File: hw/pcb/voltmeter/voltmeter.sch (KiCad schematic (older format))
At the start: 32 parts, among them J0 1935161, Q1 2N7002, Q2 2N7002, U1 SN74HC595DR, U2 TL062

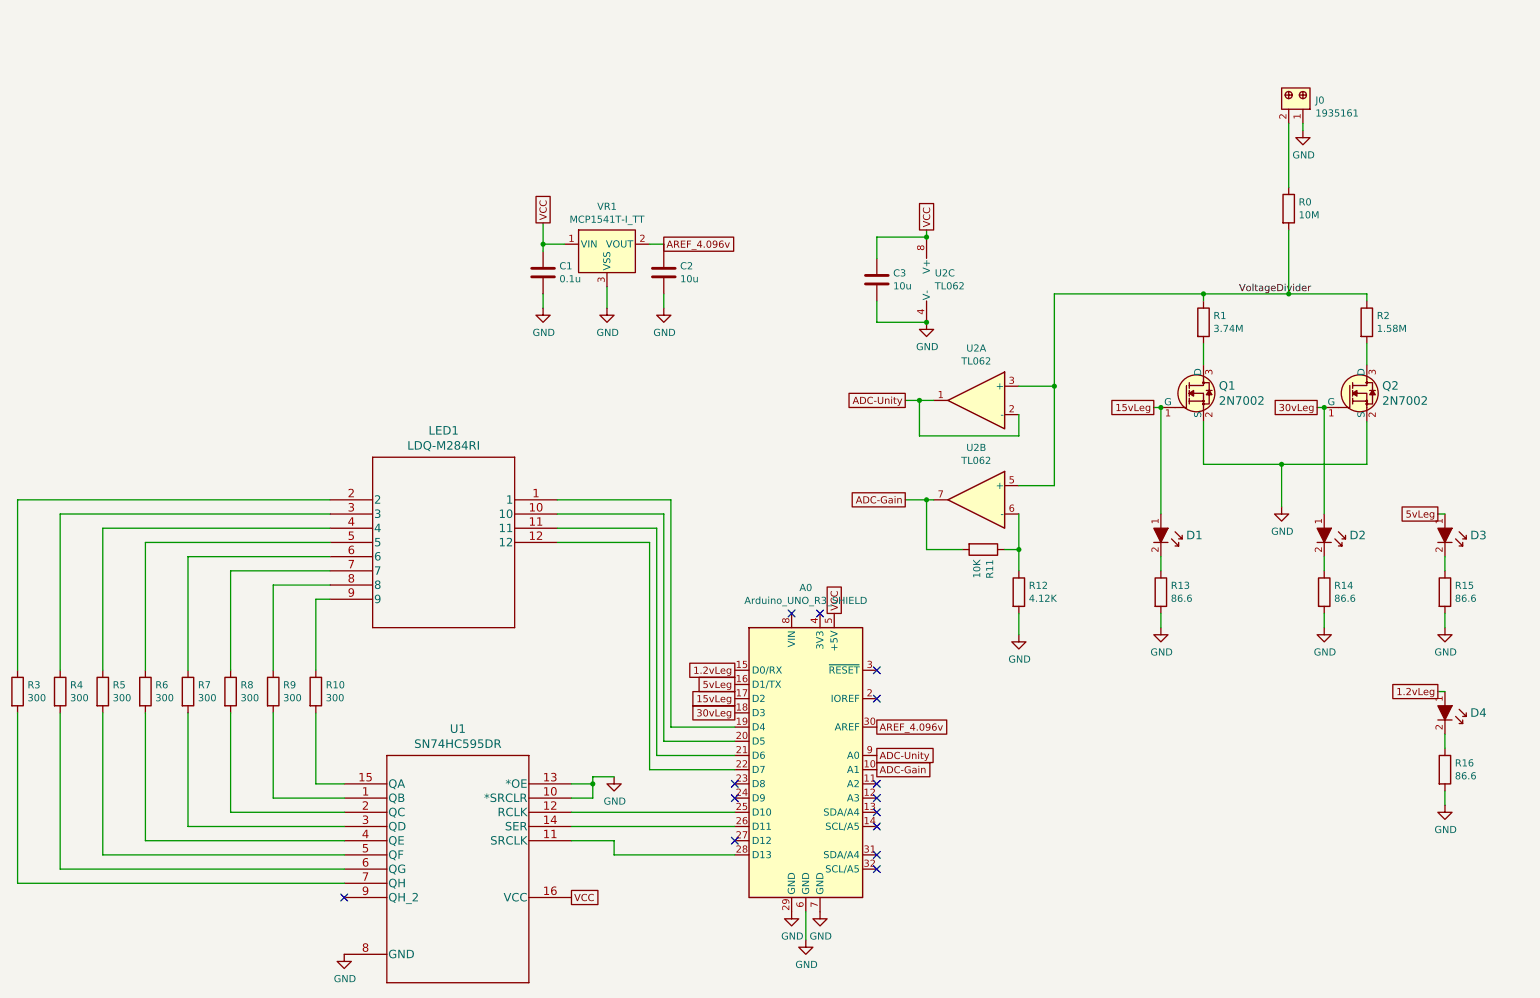
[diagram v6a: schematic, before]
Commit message: Fix incorrect 7-segment pinout.
Fixed bad 7-segment pinout. Fixed layout; regenerated gerbers.
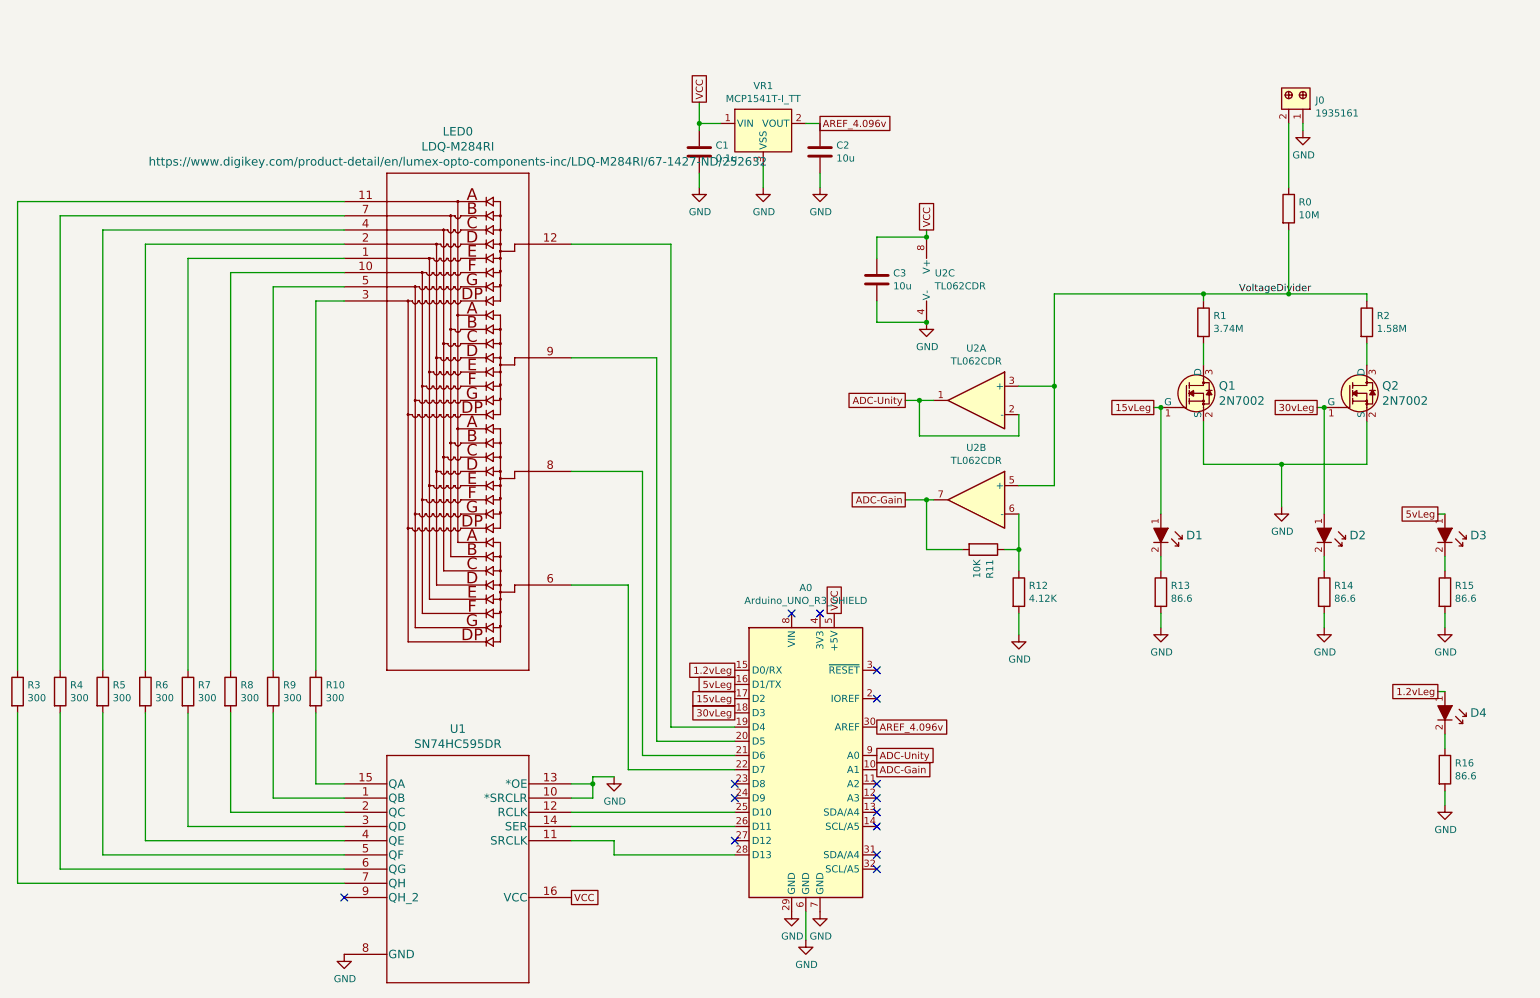
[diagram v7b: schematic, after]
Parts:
- removed LED1: LDQ-M284RI, footprints3:LDQ-M284RI, symbol 2020-08-31_02-39-33:LDQ-M284RI
- added LED0: LDQ-M284RI, footprints4:LDQ-M284RI, symbol 2020-09-17_03-48-59:LDQ-M284RI
- U2: value TL062 -> TL062CDR
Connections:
- net at A0.19 (D4): now also LED0.12
- net at A0.20 (D5): now also LED0.9
- net at A0.21 (D6): now also LED0.8
- net at A0.22 (D7): now also LED0.6
- net at R3.1: now also LED0.11
- net at R4.1: now also LED0.7
- net at R5.1: now also LED0.4
- net at R6.1: now also LED0.2
- net at R7.1: now also LED0.1
- net at R8.1: now also LED0.10
- net at R9.1: now also LED0.5
- net at R10.1: now also LED0.3
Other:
- moved on the sheet: C1, C2, VR1
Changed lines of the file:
@@
 L dk_PMIC-Voltage-Reference:MCP1541T-I_TT VR1
 U 1 1 5F4868C2
-P 4750 1700
-F 0 "VR1" H 4750 1965 50  0000 C CNN
-F 1 "MCP1541T-I_TT" H 4750 1874 50  0000 C CNN
-F 2 "digikey-footprints:SOT-23-3" H 4950 1900 60  0001 L CNN
-F 3 "http://www.microchip.com/mymicrochip/filehandler.aspx?ddocname=en011331" H 4950 2000 60  0001 L CNN
-F 4 "MCP1541T-I/TTCT-ND" H 4950 2100 60  0001 L CNN "Digi-Key_PN"
-F 5 "MCP1541T-I/TT" H 4950 2200 60  0001 L CNN "MPN"
-F 6 "Integrated Circuits (ICs)" H 4950 2300 60  0001 L CNN "Category"
-F 7 "PMIC - Voltage Reference" H 4950 2400 60  0001 L CNN "Family"
-F 8 "http://www.microchip.com/mymicrochip/filehandler.aspx?ddocname=en011331" H 4950 2500 60  0001 L CNN "DK_Datasheet_Link"
-F 9 "/product-detail/en/microchip-technology/MCP1541T-I-TT/MCP1541T-I-TTCT-ND/1979818" H 4950 2600 60  0001 L CNN "DK_Detail_Page"
-F 10 "IC VREF SERIES 4.096V SOT23-3" H 4950 2700 60  0001 L CNN "Description"
-F 11 "Microchip Technology" H 4950 2800 60  0001 L CNN "Manufacturer"
-F 12 "Active" H 4950 2900 60  0001 L CNN "Status"
-	1    4750 1700
+P 5850 850
+F 0 "VR1" H 5850 1115 50  0000 C CNN
+F 1 "MCP1541T-I_TT" H 5850 1024 50  0000 C CNN
+F 2 "digikey-footprints:SOT-23-3" H 6050 1050 60  0001 L CNN
+F 3 "http://www.microchip.com/mymicrochip/filehandler.aspx?ddocname=en011331" H 6050 1150 60  0001 L CNN
+F 4 "MCP1541T-I/TTCT-ND" H 6050 1250 60  0001 L CNN "Digi-Key_PN"
+F 5 "MCP1541T-I/TT" H 6050 1350 60  0001 L CNN "MPN"
+F 6 "Integrated Circuits (ICs)" H 6050 1450 60  0001 L CNN "Category"
+F 7 "PMIC - Voltage Reference" H 6050 1550 60  0001 L CNN "Family"
+F 8 "http://www.microchip.com/mymicrochip/filehandler.aspx?ddocname=en011331" H 6050 1650 60  0001 L CNN "DK_Datasheet_Link"
+F 9 "/product-detail/en/microchip-technology/MCP1541T-I-TT/MCP1541T-I-TTCT-ND/1979818" H 6050 1750 60  0001 L CNN "DK_Detail_Page"
+F 10 "IC VREF SERIES 4.096V SOT23-3" H 6050 1850 60  0001 L CNN "Description"
+F 11 "Microchip Technology" H 6050 1950 60  0001 L CNN "Manufacturer"
+F 12 "Active" H 6050 2050 60  0001 L CNN "Status"
+	1    5850 850
 	1    0    0    -1
 $EndComp
@@
 P 7350 2800
 F 0 "U2" H 7350 3167 50  0000 C CNN
-F 1 "TL062" H 7350 3076 50  0000 C CNN
+F 1 "TL062CDR" H 7350 3076 50  0000 C CNN
 F 2 "footprints:TL062CDR" H 7350 2800 50  0001 C CNN
-F 3 "http://www.ti.com/lit/ds/symlink/tl061.pdf" H 7350 2800 50  0001 C CNN
+F 3 "https://www.digikey.com/product-detail/en/texas-instruments/TL062CDR/296-1281-1-ND/276549" H 7350 2800 50  0001 C CNN
 	1    7350 2800
 	-1   0    0    -1
@@
 P 7350 3500
 F 0 "U2" H 7350 3867 50  0000 C CNN
-F 1 "TL062" H 7350 3776 50  0000 C CNN
+F 1 "TL062CDR" H 7350 3776 50  0000 C CNN
 F 2 "footprints:TL062CDR" H 7350 3500 50  0001 C CNN
-F 3 "http://www.ti.com/lit/ds/symlink/tl061.pdf" H 7350 3500 50  0001 C CNN
+F 3 "https://www.digikey.com/product-detail/en/texas-instruments/TL062CDR/296-1281-1-ND/276549" H 7350 3500 50  0001 C CNN
 	2    7350 3500
 	-1   0    0    -1
@@
 P 7100 1950
 F 0 "U2" H 7058 1996 50  0000 L CNN
-F 1 "TL062" H 7058 1905 50  0000 L CNN
+F 1 "TL062CDR" H 7058 1905 50  0000 L CNN
 F 2 "footprints:TL062CDR" H 7100 1950 50  0001 C CNN
-F 3 "http://www.ti.com/lit/ds/symlink/tl061.pdf" H 7100 1950 50  0001 C CNN
+F 3 "https://www.digikey.com/product-detail/en/texas-instruments/TL062CDR/296-1281-1-ND/276549" H 7100 1950 50  0001 C CNN
 	3    7100 1950
 	1    0    0    -1
@@
 L Device:C C1
 U 1 1 5F4C5E92
-P 4300 1900
-F 0 "C1" H 4415 1946 50  0000 L CNN
-F 1 "0.1u" H 4415 1855 50  0000 L CNN
-F 2 "Capacitor_SMD:C_0805_2012Metric_Pad1.15x1.40mm_HandSolder" H 4338 1750 50  0001 C CNN
-F 3 "~" H 4300 1900 50  0001 C CNN
-	1    4300 1900
+P 5400 1050
+F 0 "C1" H 5515 1096 50  0000 L CNN
+F 1 "0.1u" H 5515 1005 50  0000 L CNN
+F 2 "Capacitor_SMD:C_0805_2012Metric_Pad1.15x1.40mm_HandSolder" H 5438 900 50  0001 C CNN
+F 3 "~" H 5400 1050 50  0001 C CNN
+	1    5400 1050
 	1    0    0    -1
 $EndComp
@@
 L Device:C C2
 U 1 1 5F4C90BC
-P 5150 1900
-F 0 "C2" H 5265 1946 50  0000 L CNN
-F 1 "10u" H 5265 1855 50  0000 L CNN
-F 2 "Capacitor_SMD:C_0805_2012Metric_Pad1.15x1.40mm_HandSolder" H 5188 1750 50  0001 C CNN
-F 3 "~" H 5150 1900 50  0001 C CNN
-	1    5150 1900
+P 6250 1050
+F 0 "C2" H 6365 1096 50  0000 L CNN
+F 1 "10u" H 6365 1005 50  0000 L CNN
+F 2 "Capacitor_SMD:C_0805_2012Metric_Pad1.15x1.40mm_HandSolder" H 6288 900 50  0001 C CNN
+F 3 "~" H 6250 1050 50  0001 C CNN
+	1    6250 1050
 	1    0    0    -1
 $EndComp
@@
 L power:GND #PWR0109
 U 1 1 5F4CBE9E
-P 4750 2150
-F 0 "#PWR0109" H 4750 1900 50  0001 C CNN
-F 1 "GND" H 4755 1977 50  0000 C CNN
-F 2 "" H 4750 2150 50  0001 C CNN
-F 3 "" H 4750 2150 50  0001 C CNN
-	1    4750 2150
+P 5850 1300
+F 0 "#PWR0109" H 5850 1050 50  0001 C CNN
+F 1 "GND" H 5855 1127 50  0000 C CNN
+F 2 "" H 5850 1300 50  0001 C CNN
+F 3 "" H 5850 1300 50  0001 C CNN
+	1    5850 1300
 	1    0    0    -1
 $EndComp
@@
 	1    0    0    -1
 $EndComp
-Text GLabel 4300 1550 1    50   UnSpc ~ 0
+Text GLabel 5400 700  1    50   UnSpc ~ 0
 VCC
 Wire Wire Line
-	4300 1550 4300 1700
-Wire Wire Line
-	4450 1700 4300 1700
-Connection ~ 4300 1700
-Wire Wire Line
-	4300 1700 4300 1750
-Wire Wire Line
-	4300 2050 4300 2150
-Wire Wire Line
-	4750 2000 4750 2150
+	5400 700  5400 850
+Wire Wire Line
+	5550 850  5400 850
+Connection ~ 5400 850
+Wire Wire Line
+	5400 850  5400 900
+Wire Wire Line
+	5400 1200 5400 1300
+Wire Wire Line
+	5850 1150 5850 1300
 $Comp
 L power:GND #PWR0111
 U 1 1 5F4D0D65
-P 5150 2150
-F 0 "#PWR0111" H 5150 1900 50  0001 C CNN
-F 1 "GND" H 5155 1977 50  0000 C CNN
-F 2 "" H 5150 2150 50  0001 C CNN
-F 3 "" H 5150 2150 50  0001 C CNN
-	1    5150 2150
-	1    0    0    -1
-$EndComp
-Wire Wire Line
-	5050 1700 5150 1700
-Wire Wire Line
-	5150 1700 5150 1750
-Wire Wire Line
-	5150 2050 5150 2150
-Text GLabel 5150 1700 2    50   UnSpc ~ 0
+P 6250 1300
+F 0 "#PWR0111" H 6250 1050 50  0001 C CNN
+F 1 "GND" H 6255 1127 50  0000 C CNN
+F 2 "" H 6250 1300 50  0001 C CNN
+F 3 "" H 6250 1300 50  0001 C CNN
+	1    6250 1300
+	1    0    0    -1
+$EndComp
+Wire Wire Line
+	6150 850  6250 850
+Wire Wire Line
+	6250 850  6250 900
+Wire Wire Line
+	6250 1200 6250 1300
+Text GLabel 6250 850  2    50   UnSpc ~ 0
 AREF_4.096v
 Text GLabel 6650 5100 2    50   UnSpc ~ 0
@@
 	1    0    0    -1
 $EndComp
-$Comp
-L 2020-08-31_02-39-33:LDQ-M284RI LED1
-U 1 1 5F5292F1
-P 2800 3500
-F 0 "LED1" H 3600 3987 60  0000 C CNN
-F 1 "LDQ-M284RI" H 3600 3881 60  0000 C CNN
-F 2 "footprints3:LDQ-M284RI" H 3600 3840 60  0001 C CNN
-F 3 "https://www.digikey.com/product-detail/en/lumex-opto-components-inc/LDQ-M284RI/67-1427-ND/252632" H 2800 3500 60  0001 C CNN
-	1    2800 3500
-	1    0    0    -1
-$EndComp
 Wire Wire Line
 	4500 5700 5650 5700
@@
 Wire Wire Line
 	5650 5100 5200 5100
-Wire Wire Line
-	5200 5100 5200 3500
-Wire Wire Line
-	5200 3500 4400 3500
-Wire Wire Line
-	4400 3600 5150 3600
-Wire Wire Line
-	5150 3600 5150 5200
-Wire Wire Line
-	5150 5200 5650 5200
-Wire Wire Line
-	5650 5300 5100 5300
-Wire Wire Line
-	5100 5300 5100 3700
-Wire Wire Line
-	5100 3700 4400 3700
-Wire Wire Line
-	4400 3800 5050 3800
-Wire Wire Line
-	5050 3800 5050 5400
-Wire Wire Line
-	5050 5400 5650 5400
 $Comp
 L Device:R R3
@@
 L power:GND #PWR0114
 U 1 1 5F54862D
-P 4300 2150
-F 0 "#PWR0114" H 4300 1900 50  0001 C CNN
-F 1 "GND" H 4305 1977 50  0000 C CNN
-F 2 "" H 4300 2150 50  0001 C CNN
-F 3 "" H 4300 2150 50  0001 C CNN
-	1    4300 2150
+P 5400 1300
+F 0 "#PWR0114" H 5400 1050 50  0001 C CNN
+F 1 "GND" H 5405 1127 50  0000 C CNN
+F 2 "" H 5400 1300 50  0001 C CNN
+F 3 "" H 5400 1300 50  0001 C CNN
+	1    5400 1300
 	1    0    0    -1
 $EndComp
@@
 	600  6200 600  5000
 Wire Wire Line
-	2700 4700 2700 4200
-Wire Wire Line
-	2700 4200 2800 4200
-Wire Wire Line
-	2800 4100 2400 4100
-Wire Wire Line
-	2400 4100 2400 4700
-Wire Wire Line
-	2800 4000 2100 4000
-Wire Wire Line
-	2100 4000 2100 4700
-Wire Wire Line
-	2800 3900 1800 3900
-Wire Wire Line
-	1800 3900 1800 4700
-Wire Wire Line
-	2800 3800 1500 3800
-Wire Wire Line
-	1500 3800 1500 4700
-Wire Wire Line
-	2800 3700 1200 3700
-Wire Wire Line
-	1200 3700 1200 4700
-Wire Wire Line
-	2800 3600 900  3600
-Wire Wire Line
-	900  3600 900  4700
-Wire Wire Line
-	2800 3500 600  3500
-Wire Wire Line
-	600  3500 600  4700
-Wire Wire Line
 	9800 4300 9800 4400
 $Comp
@@
 	1    0    0    -1
 $EndComp
+$Comp
+L 2020-09-17_03-48-59:LDQ-M284RI LED0
+U 1 1 5F6E9FDC
+P 2900 1400
+F 0 "LED0" H 3700 1893 60  0000 C CNN
+F 1 "LDQ-M284RI" H 3700 1787 60  0000 C CNN
+F 2 "footprints4:LDQ-M284RI" H 3700 1640 60  0001 C CNN
+F 3 "https://www.digikey.com/product-detail/en/lumex-opto-components-inc/LDQ-M284RI/67-1427-ND/252632" H 3700 1681 60  0000 C CNN
+	1    2900 1400
+	1    0    0    -1
+$EndComp
+Wire Wire Line
+	2900 2100 2700 2100
+Wire Wire Line
+	2700 2100 2700 4700
+Wire Wire Line
+	2400 2000 2900 2000
+Wire Wire Line
+	2400 2000 2400 4700
+Wire Wire Line
+	2900 1900 2100 1900
+Wire Wire Line
+	2100 1900 2100 4700
+Wire Wire Line
+	1800 1800 2900 1800
+Wire Wire Line
+	1800 1800 1800 4700
+Wire Wire Line
+	2900 1700 1500 1700
+Wire Wire Line
+	1500 1700 1500 4700
+Wire Wire Line
+	2900 1600 1200 1600
+Wire Wire Line
+	1200 1600 1200 4700
+Wire Wire Line
+	900  1500 2900 1500
+Wire Wire Line
+	900  1500 900  4700
+Wire Wire Line
+	2900 1400 600  1400
+Wire Wire Line
+	600  1400 600  4700
+Wire Wire Line
+	4900 5400 4900 4100
+Wire Wire Line
+	4900 4100 4500 4100
+Wire Wire Line
+	4900 5400 5650 5400
+Wire Wire Line
+	5000 5300 5000 3300
+Wire Wire Line
+	5000 3300 4500 3300
+Wire Wire Line
+	5000 5300 5650 5300
+Wire Wire Line
+	5100 5200 5100 2500
+Wire Wire Line
+	5100 2500 4500 2500
+Wire Wire Line
+	5100 5200 5650 5200
+Wire Wire Line
+	5200 5100 5200 1700
+Wire Wire Line
+	5200 1700 4500 1700
 $EndSCHEMATC

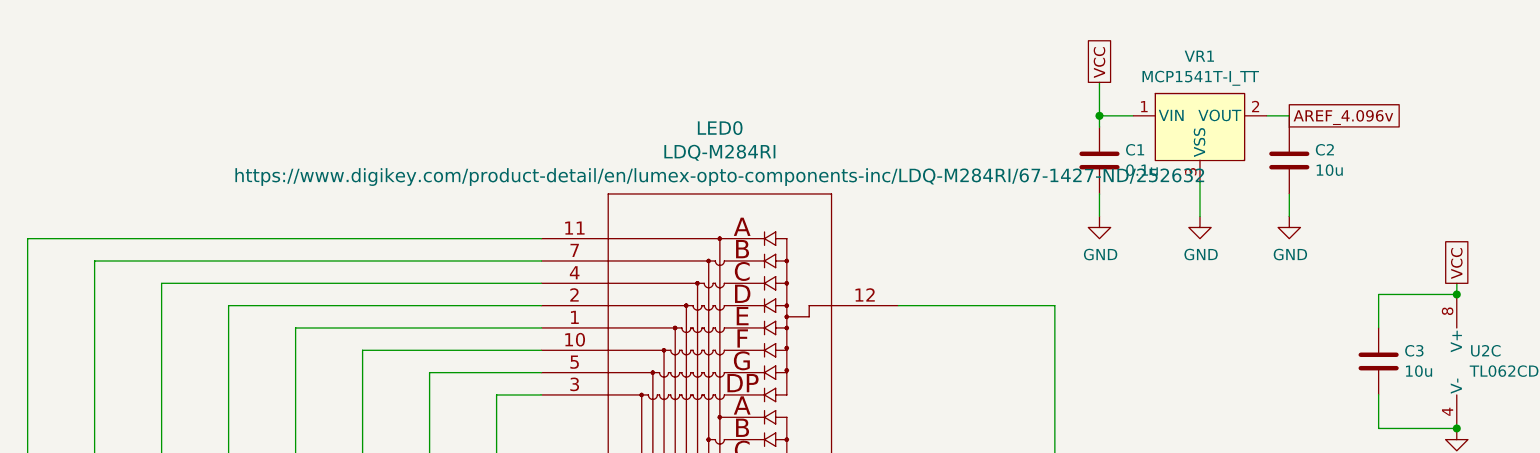
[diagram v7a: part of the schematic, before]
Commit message: Finalize board for order.
Finalized BOM, saved BOM from DigiKey.
Updated layout to match updated BOM.
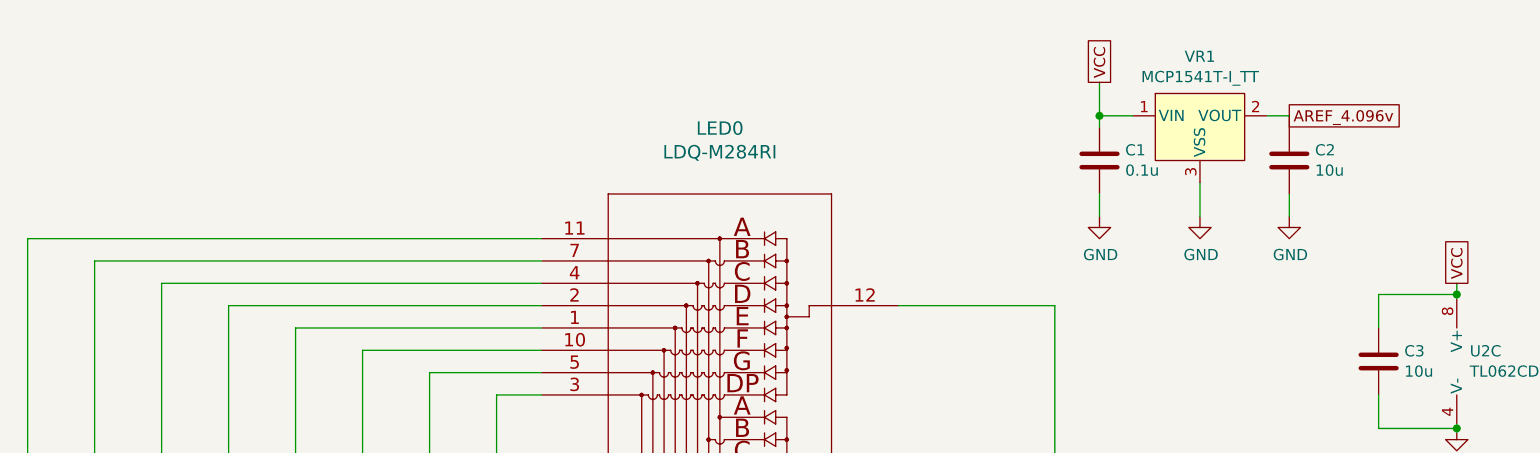
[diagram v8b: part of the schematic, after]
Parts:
- C2, C3: footprint Capacitor_SMD:C_0805_2012Metric_Pad1.15x1.40mm_HandSolder -> Capacitor_SMD:C_1210_3225Metric_Pad1.42x2.65mm_HandSolder
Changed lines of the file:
@@
-$EndComp
-$Comp
-L Device:C C2
-U 1 1 5F4C90BC
-P 6250 1050
-F 0 "C2" H 6365 1096 50  0000 L CNN
-F 1 "10u" H 6365 1005 50  0000 L CNN
-F 2 "Capacitor_SMD:C_0805_2012Metric_Pad1.15x1.40mm_HandSolder" H 6288 900 50  0001 C CNN
-F 3 "~" H 6250 1050 50  0001 C CNN
-	1    6250 1050
-	1    0    0    -1
 $EndComp
 $Comp
@@
 F 0 "C3" H 6765 1996 50  0000 L CNN
 F 1 "10u" H 6765 1905 50  0000 L CNN
-F 2 "Capacitor_SMD:C_0805_2012Metric_Pad1.15x1.40mm_HandSolder" H 6688 1800 50  0001 C CNN
+F 2 "Capacitor_SMD:C_1210_3225Metric_Pad1.42x2.65mm_HandSolder" H 6688 1800 50  0001 C CNN
 F 3 "~" H 6650 1950 50  0001 C CNN
 	1    6650 1950
@@
 F 1 "LDQ-M284RI" H 3700 1787 60  0000 C CNN
 F 2 "footprints4:LDQ-M284RI" H 3700 1640 60  0001 C CNN
-F 3 "https://www.digikey.com/product-detail/en/lumex-opto-components-inc/LDQ-M284RI/67-1427-ND/252632" H 3700 1681 60  0000 C CNN
+F 3 "https://www.digikey.com/product-detail/en/lumex-opto-components-inc/LDQ-M284RI/67-1427-ND/252632" H 3700 1681 60  0001 C CNN
 	1    2900 1400
 	1    0    0    -1
@@
 Wire Wire Line
 	5200 1700 4500 1700
+$Comp
+L Device:C C2
+U 1 1 5F4C90BC
+P 6250 1050
+F 0 "C2" H 6365 1096 50  0000 L CNN
+F 1 "10u" H 6365 1005 50  0000 L CNN
+F 2 "Capacitor_SMD:C_1210_3225Metric_Pad1.42x2.65mm_HandSolder" H 6288 900 50  0001 C CNN
+F 3 "~" H 6250 1050 50  0001 C CNN
+	1    6250 1050
+	1    0    0    -1
+$EndComp
 $EndSCHEMATC
